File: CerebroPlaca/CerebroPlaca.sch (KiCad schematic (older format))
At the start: 39 parts

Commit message: se queda con el USB-C
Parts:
- removed J?: USB_OTG-nrfmicro-rescue, symbol cerebro-rescue:USB_OTG-nrfmicro-rescue
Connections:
- no-connect marks 7 -> 5
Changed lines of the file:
@@
 P0.26
-$Comp
-L cerebro-rescue:USB_OTG-nrfmicro-rescue J?
-U 1 1 5E504B1F
-P 5400 1700
-F 0 "J?" H 5457 2167 50  0000 C CNN
-F 1 "USB_OTG-nrfmicro-rescue" H 5457 2076 50  0000 C CNN
-F 2 "" H 5550 1650 50  0001 C CNN
-F 3 "" H 5550 1650 50  0001 C CNN
-	1    5400 1700
-	1    0    0    -1
-$EndComp
 $Comp
 L Connector:USB_C_Receptacle_USB2.0 J?
@@
 	7900 1600 7800 1600
 Connection ~ 7900 1550
-NoConn ~ 5300 2100
-NoConn ~ 5700 1900
-$Comp
-L nrfmicro-rescue:GND #PWR0115
-U 1 1 5E52C5DE
-P 5500 2100
-F 0 "#PWR0115" H 5500 1850 50  0001 C CNN
-F 1 "GND" V 5505 1972 50  0000 R CNN
-F 2 "" H 5500 2100 50  0001 C CNN
-F 3 "" H 5500 2100 50  0001 C CNN
-	1    5500 2100
-	0    -1   -1   0
-$EndComp
-Wire Wire Line
-	5500 2100 5400 2100
-Text GLabel 5800 1800 2    50   Input ~ 0
-DATA-
-Text GLabel 5800 1700 2    50   Input ~ 0
-DATA+
-Wire Wire Line
-	5700 1700 5800 1700
-Wire Wire Line
-	5800 1800 5700 1800
-Text GLabel 5800 1500 2    50   Input ~ 0
-VBUS
-Wire Wire Line
-	5800 1500 5700 1500
 $Comp
 L cerebro-cache:Connector_Generic_Conn_01x02 J?

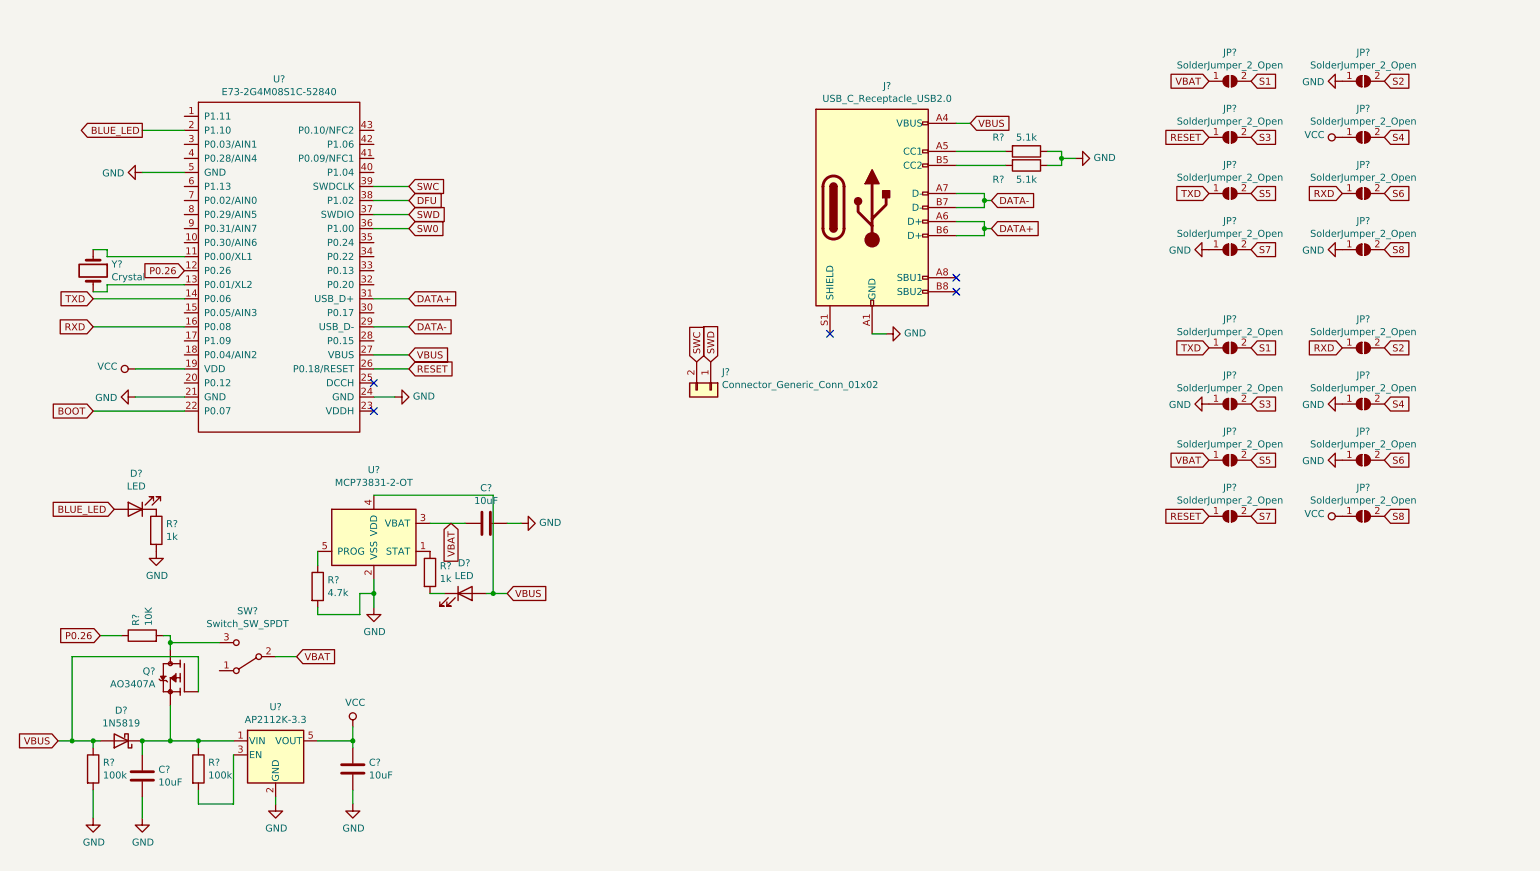
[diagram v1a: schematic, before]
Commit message: Cambio de esquemático en placa cerebro, con prueba de placa de la mima carpeta
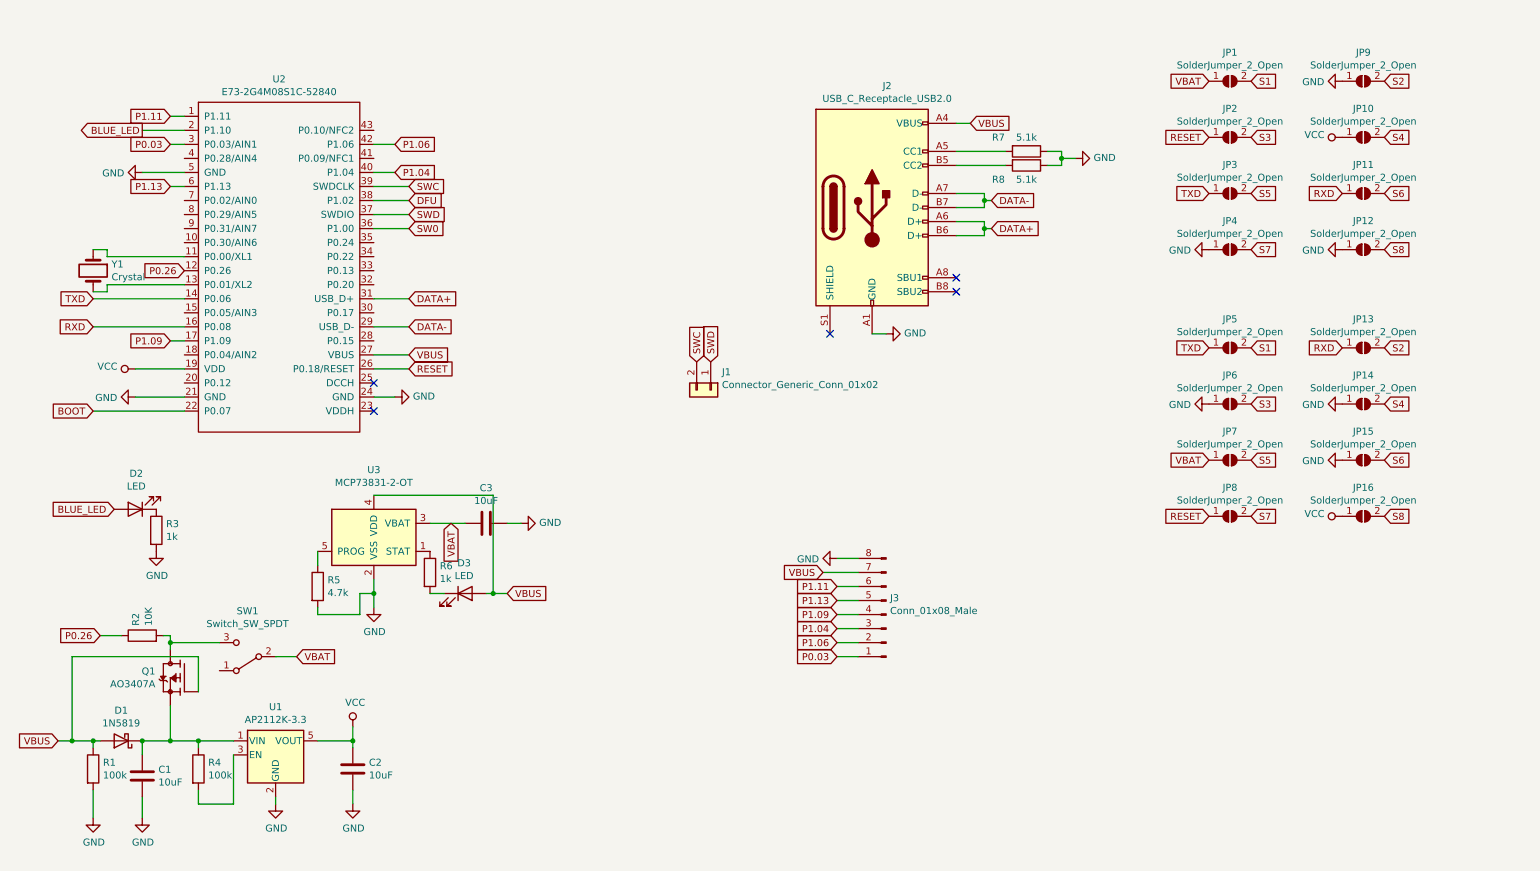
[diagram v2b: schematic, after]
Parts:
- added J3: Conn_01x08_Male, cerebro:coenctor_8-(4-4), symbol Connector:Conn_01x08_Male
- C1, C2, C3: renamed from C?; footprint (none) -> Capacitor_SMD:C_0805_2012Metric
- D1: renamed from D?; footprint Diode_THT:D_DO-41_SOD81_P10.16mm_Horizontal -> Diode_SMD:D_SOD-123F
- D2, D3: renamed from D?; footprint (none) -> LED_SMD:LED_0603_1608Metric
- J1: renamed from J?; footprint (none) -> nrfmicro:connector_swd
- J2: renamed from J?; footprint (none) -> nrfmicro:usb_type_c
- Q1: renamed from Q?; footprint SOT95P280X125-3N -> Package_TO_SOT_SMD:SOT-23
- R1, R2, R3, R4, R5, R6, R7, R8: renamed from R?; footprint (none) -> Resistor_SMD:R_0603_1608Metric
- SW1: renamed from SW?; footprint (none) -> nrfmicro:switch_MSK-12C02_smd
- U2: renamed from U?; footprint (none) -> nrfmicro:E73-2G4M08S1C
- Y1: renamed from Y?; footprint (none) -> Crystal:Crystal_Round_D1.0mm_Vertical
- gave numbers to parts that had none: 18
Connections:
- net GND: now also J3.8 (Pin_8)
- net VBUS: now also J3.7 (Pin_7)
- net P1.11: now reaches U2.1 (P1.11)
- net P1.11: now also J3.6 (Pin_6)
- net P1.09: now reaches U2.17 (P1.09)
- net P1.09: now also J3.4 (Pin_4)
- net P0.03: now reaches U2.3 (P0.03/AIN1)
- net P0.03: now also J3.1 (Pin_1)
- net P1.04: now reaches U2.40 (P1.04)
- net P1.04: now also J3.3 (Pin_3)
- net P1.06: now reaches U2.42 (P1.06)
- net P1.06: now also J3.2 (Pin_2)
- net P1.13: now reaches U2.6 (P1.13)
- net P1.13: now also J3.5 (Pin_5)

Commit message: ajustes en placaCerebro
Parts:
- removed J1: Connector_Generic_Conn_01x02, nrfmicro:connector_swd, symbol cerebro-cache:Connector_Generic_Conn_01x02
- removed JP1, JP10, JP11, JP12, JP13, JP14, JP15, JP16, JP2, JP3, JP4, JP5, JP6, JP7, JP8, JP9: SolderJumper_2_Open, nrfmicro:jumper, symbol Jumper:SolderJumper_2_Open
- added J1: Conn_01x04_Male, Connector_PinHeader_1.00mm:PinHeader_1x04_P1.00mm_Vertical, symbol Connector:Conn_01x04_Male
- added L1: 10uH, Inductor_SMD:L_7.3x7.3_H3.5, symbol Device:L
- added SW2: RESET, Button_Switch_SMD:SW_SPST_TL3342, symbol Switch:SW_MEC_5G
- Y1: value Crystal -> 32Khz
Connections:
- net VCC is gone; now on net +3V3: C2.1, U1.5 (VOUT), U2.19 (VDD)
- net GND: now also J1.4 (Pin_4), SW2.1 (A), SW2.2 (A)
- net P1.13: no longer J3.5 (Pin_5), U2.6 (P1.13)
- net VBUS: no longer J3.7 (Pin_7)
- net PWDN: now reaches U2.10 (P0.30/AIN6)
- net +3V3: now reaches U2.23 (VDDH)
- net +3V3: now also J3.7 (Pin_7), J1.1 (Pin_1), L1.2
- net at U2.25 (DCCH): now also L1.1
- net MISO: now reaches U2.28 (P0.15)
- net P0.20: now reaches U2.32 (P0.20)
- net P0.20: now also J3.5 (Pin_5)
- net P0.13: now reaches U2.33 (P0.13)
- net P0.13: now also J3.2 (Pin_2)
- net RSTB: now reaches U2.4 (P0.28/AIN4)
- net CS: now reaches U2.7 (P0.02/AIN0)
- net START: now reaches U2.8 (P0.29/AIN5)
- net DRDY: now reaches U2.9 (P0.31/AIN7)
- net BLUE_LED renamed LED
- net DATA+ renamed D+
- net DATA- renamed D-
- net DFU: no longer names the net of U2.38 (P1.02)
- net P1.06 renamed MOSI
- net MOSI: no longer J3.2 (Pin_2)
- net RESET renamed RST
- net RST: now also SW2.3 (B), SW2.4 (B)
- net SWC renamed SWDCLK
- net SWD renamed SWDIO
- net SWDIO: now also J1.2 (Pin_2)
- net VBAT renamed +BATT
- new net SCK: U2.6 (P1.13)
- new net SWCLK: J1.3 (Pin_3)
- no-connect marks 5 -> 13
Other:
- note added: "BATTERY CHARGER"
- note added: "MICRONTROLLER"
- note added: "PLUS CONNECTIONS"
- note added: "REGULATOR AND FILTERS"
- note added: "USB & MISSELANOUS"
- moved on the sheet: C1, C2, C3, D1, D2, D3, J3, Q1, R1, R2, R3, R4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
